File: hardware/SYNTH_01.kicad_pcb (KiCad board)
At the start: 2 copper layers, 114.5 x 158 mm, 61 parts, among them J2 Conn_01x04_Pin, SW1 SW_Push_45deg, SW10 SW_Push_45deg, SW11 SW_Push_45deg, SW12 SW_Push_45deg, SW13 SW_Push_45deg, SW14 SW_Push_45deg, SW15 SW_Push_45deg, SW16 SW_Push_45deg, SW17 SW_Push_45deg, SW18 SW_Push_45deg, SW19 SW_Push_45deg, SW2 SW_Push_45deg, SW20 SW_Push_45deg, SW21 SW_Push_45deg, SW3 SW_Push_45deg, SW4 SW_Push_45deg, SW5 SW_Push_45deg, SW6 SW_Push_45deg, SW7 SW_Push_45deg, SW8 SW_Push_45deg, SW9 SW_Push_45deg, U1 MCP23017-E/SP

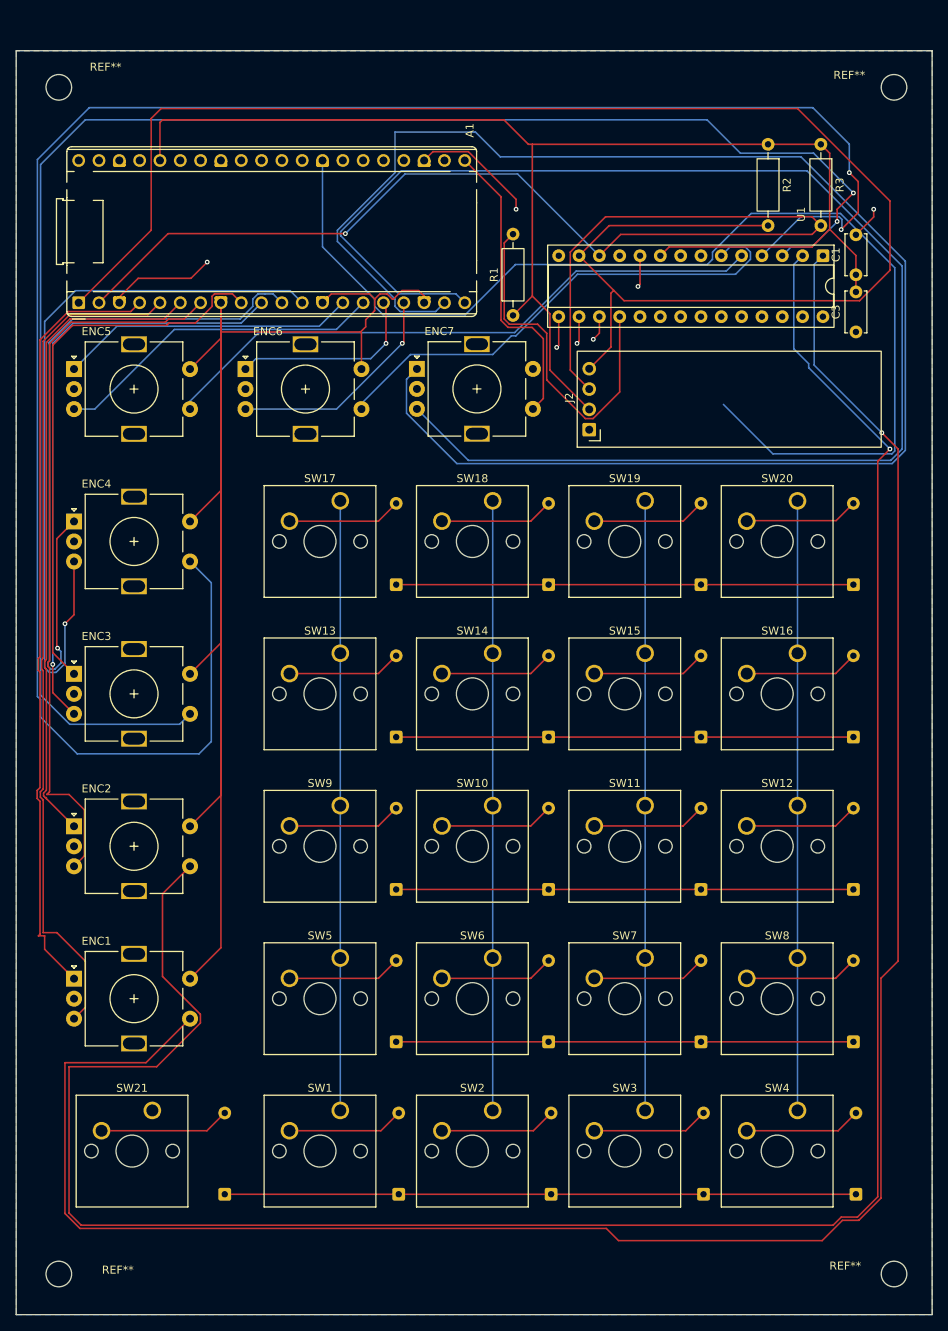
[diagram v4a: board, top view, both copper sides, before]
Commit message: fix(pcb): route matrix and clear DRC
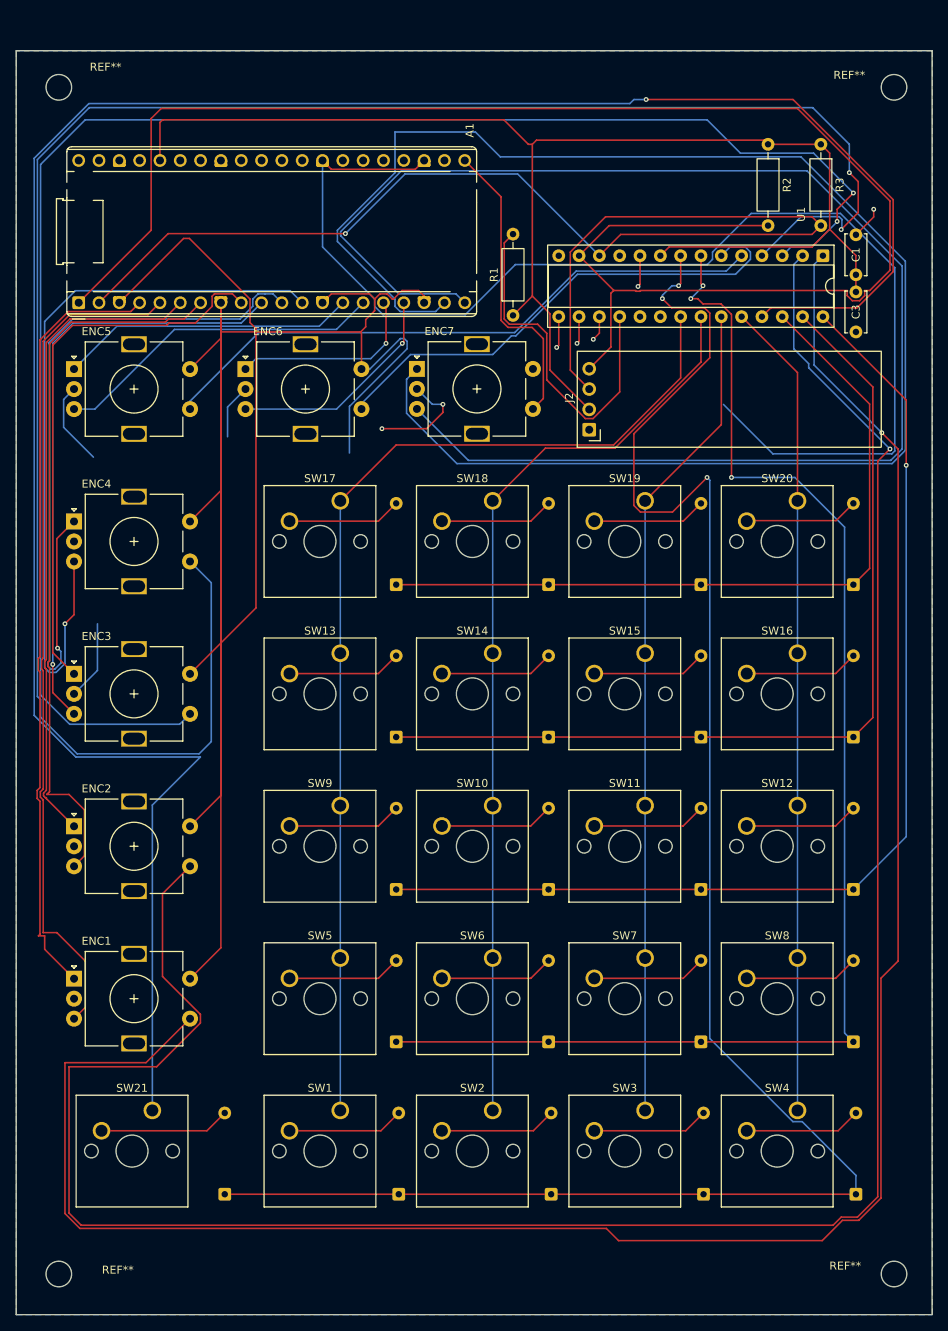
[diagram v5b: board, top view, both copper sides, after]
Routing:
- net /COL_SHIFT: track 0.00 -> 282.6 mm, vias 0 -> 1
- net /ROW4: track 78.9 -> 229.6 mm, vias 0 -> 3
- net GND: track 472.6 -> 591.6 mm
- net /ROW3: track 57.1 -> 171.0 mm, vias 0 -> 3
- net /ROW2: track 57.1 -> 135.8 mm, vias 0 -> 1
- net /ROW1: track 57.1 -> 114.3 mm
- net /COL0: track 76.2 -> 132.8 mm
- net /COL1: track 76.2 -> 115.1 mm
- net /ROW0: track 57.1 -> 96.0 mm
- net /COL2: track 76.2 -> 103.2 mm
- net /COL3: track 76.3 -> 102.2 mm
- net /SDA: track 212.1 -> 212.9 mm

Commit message: Adding midi din-5 connection
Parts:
- added J1: DIN-5_180degree, SYNTH_01_fp:MIDI_DIN5, F.Cu at (120.8, 30.6)
- added R4: 33, Resistor_THT:R_Axial_DIN0207_L6.3mm_D2.5mm_P10.16mm_Horizontal, F.Cu at (132.5, 26.4)
- added R5: 10, Resistor_THT:R_Axial_DIN0207_L6.3mm_D2.5mm_P10.16mm_Horizontal, F.Cu at (132.5, 30.5)
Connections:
- A1 pad 34: unconnected-(A1-GPIO28_ADC2-Pad34) -> /midi_data
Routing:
- net /midi_data: track 0.00 -> 124.5 mm, vias 0 -> 2
- net +3V3: track 171.5 -> 242.0 mm, vias 0 -> 2
- net Net-(J1-Pad5): track 0.00 -> 34.5 mm
- net /SDA: track 212.9 -> 238.3 mm
- net Net-(J1-Pad4): track 0.00 -> 17.4 mm
- net /E4_SW: track 248.9 -> 262.7 mm
- net /E3_SW: track 207.8 -> 219.7 mm
- net /COL_SHIFT: track 282.6 -> 293.2 mm
- net /E7_B: track 184.6 -> 187.4 mm
- net /E7_A: track 200.5 -> 203.4 mm
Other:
- board size 114.5 x 158 mm -> 114.5 x 162.3 mm
